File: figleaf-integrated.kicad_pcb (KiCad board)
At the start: 2 copper layers, 145 x 106 mm, 70 parts, among them J1 Conn_01x02_Pin, J2 HRO_TYPE-C-31-M-14, J3 Battery, J9 TC2030_SWD, Q2 2N7002, SW1 PWR, SW2 RST, U1 SRV05-4, U10 MAX17048, U3 BQ24075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

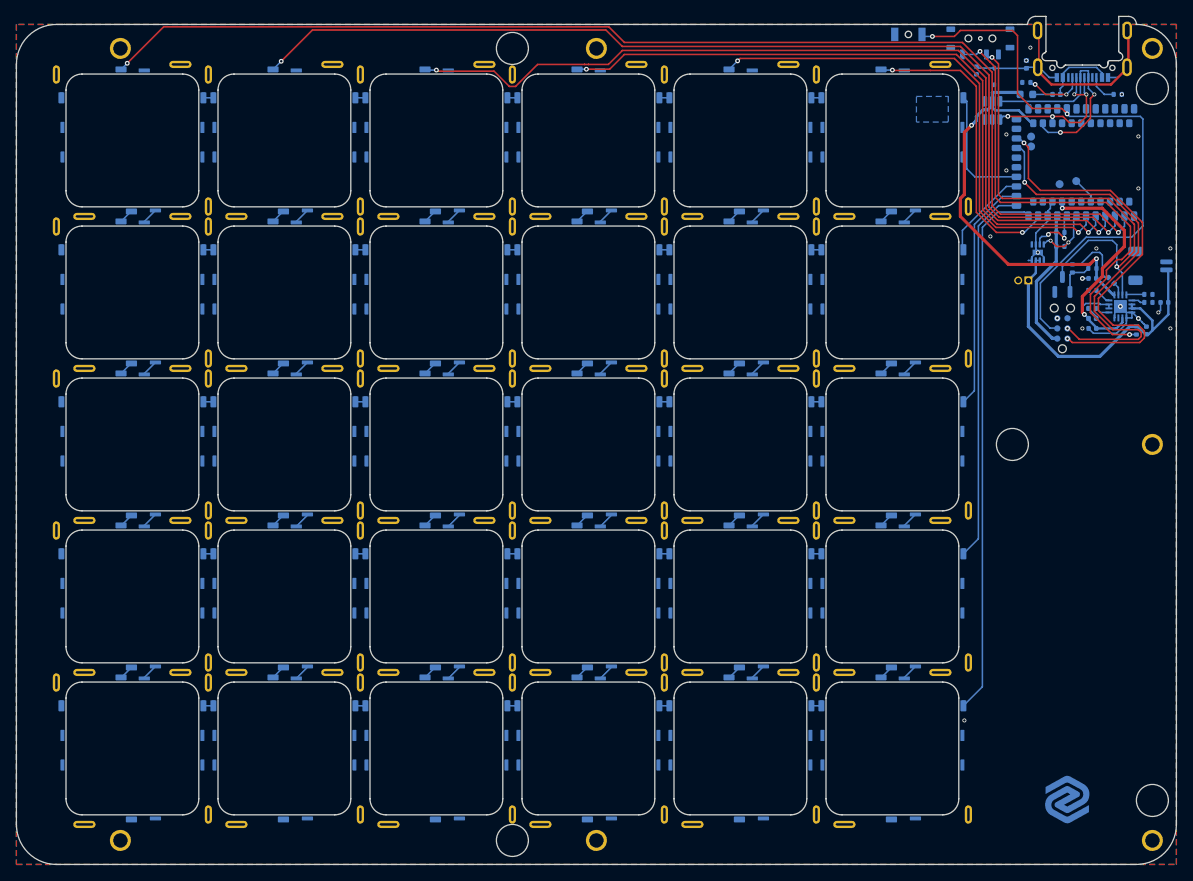
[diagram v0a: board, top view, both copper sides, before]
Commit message: Move LED near antenna
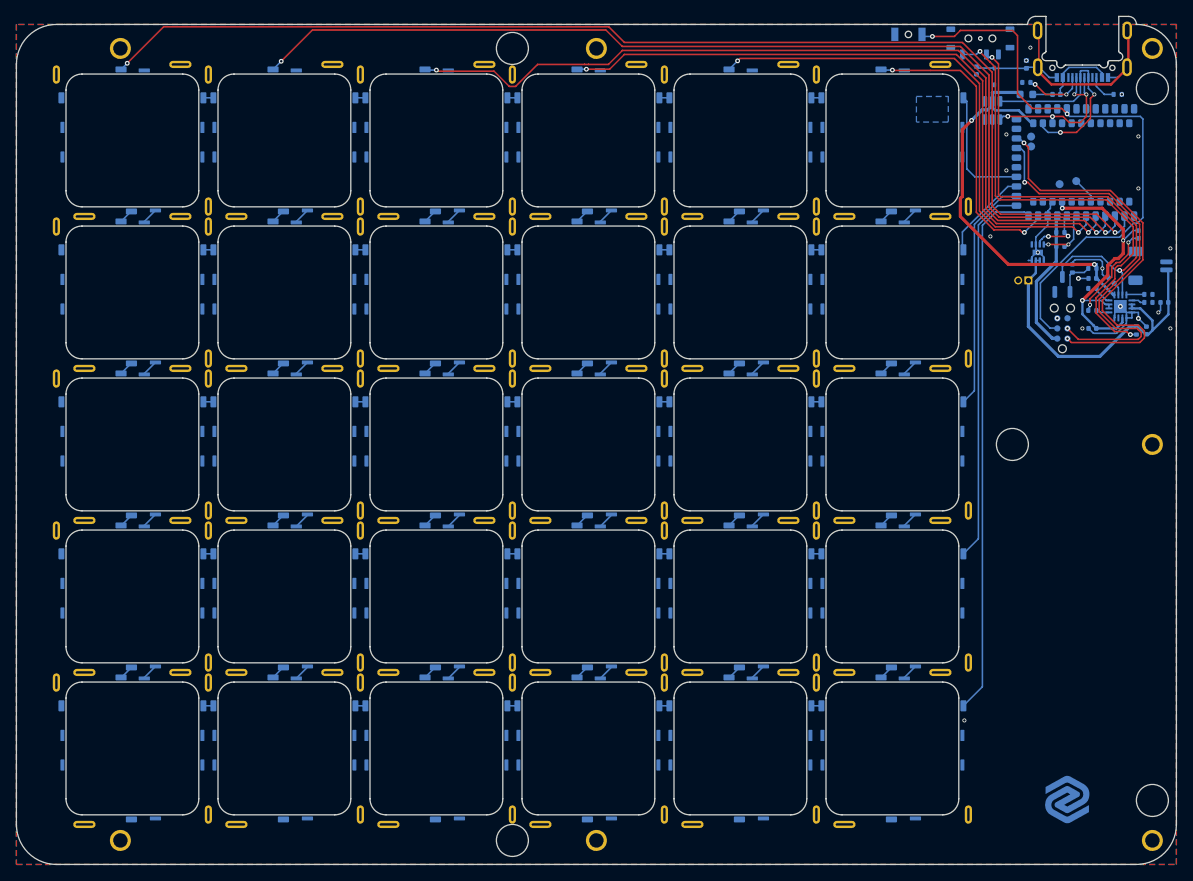
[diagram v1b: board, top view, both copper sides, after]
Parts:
- moved LED2 12.0 mm to (152.7, 38.8), turned to 90 degrees
- moved R10 0.25 mm to (147.0, 48.2)
- moved R12 0.25 mm to (147.0, 45.5)
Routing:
- net Net-(LED2-K): track 1.66 -> 12.0 mm, vias 0 -> 2
- net SYSOFF: track 59.5 -> 56.9 mm
- net +VSW: track 34.1 -> 35.7 mm, vias 2 -> 3
- net +5V: track 53.3 -> 52.3 mm
- net SWDCLK: track 52.1 -> 51.3 mm
- net Net-(SW1-A): track 59.8 -> 59.2 mm
- net RST: track 73.7 -> 73.1 mm
- net SWDIO: track 53.3 -> 52.7 mm
- net SDA: track 8.20 -> 7.65 mm

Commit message: small deets
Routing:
- net RST: track 73.1 -> 72.1 mm

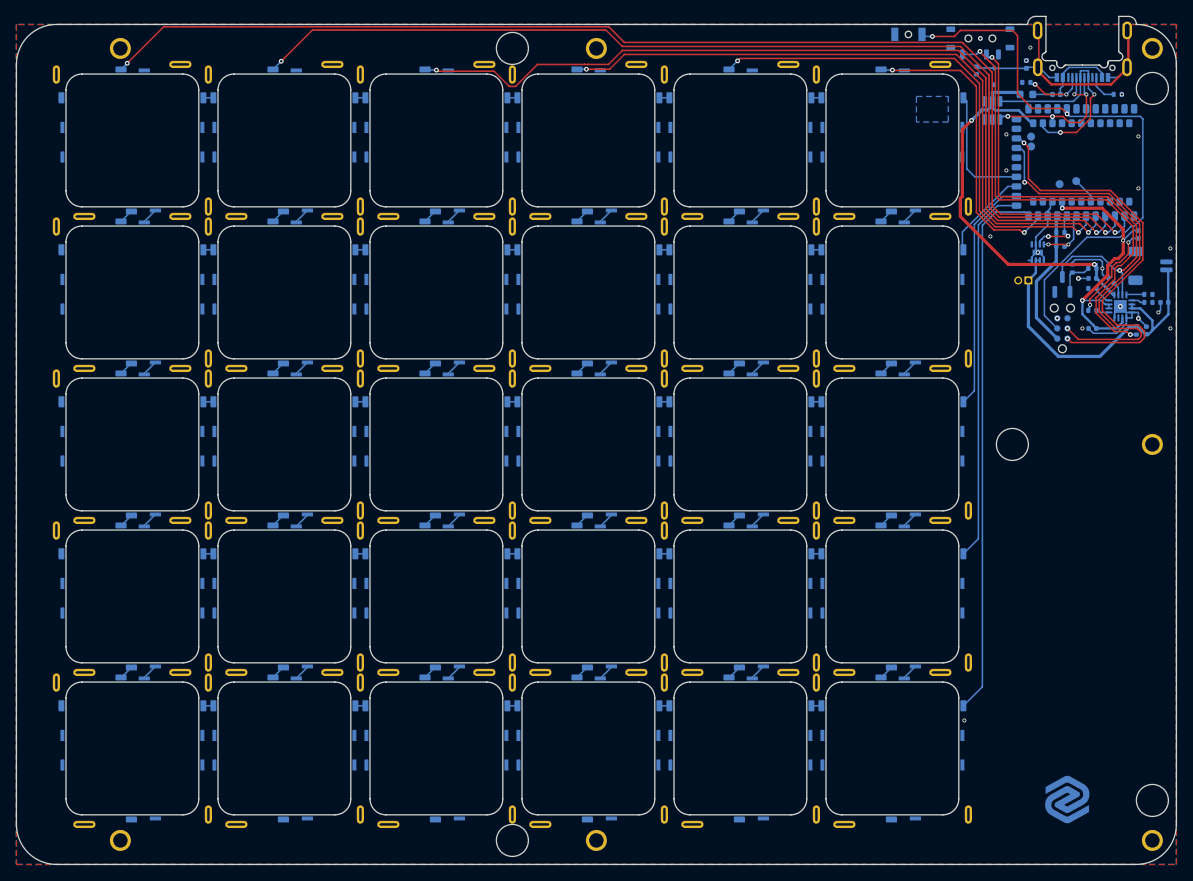
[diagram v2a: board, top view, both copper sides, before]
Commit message: update OKM footprint, larger GND, smaller RADI
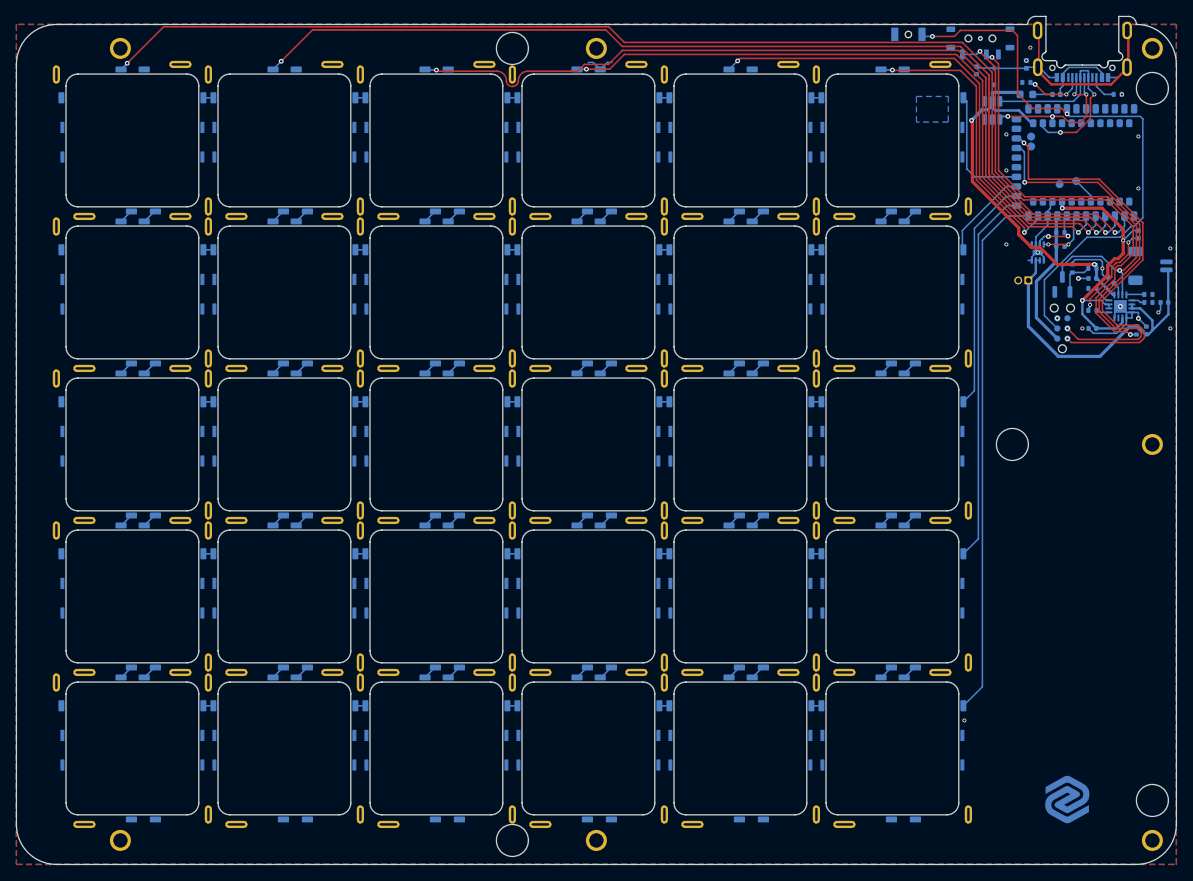
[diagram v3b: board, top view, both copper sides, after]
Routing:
- net +5V: track 52.3 -> 48.2 mm
- net GND_L: track 39.2 -> 42.9 mm
- net col_1: track 129.4 -> 127.0 mm
- net col_0: track 150.0 -> 147.6 mm
- net col_4: track 65.4 -> 63.0 mm
- net col_3: track 85.9 -> 83.5 mm
- net col_5: track 38.3 -> 36.3 mm
- net col_2: track 108.5 -> 106.5 mm
- net Net-(SW1-A): track 59.2 -> 57.4 mm
- net SYSOFF: track 56.9 -> 55.1 mm
- net row_4: track 67.7 -> 66.2 mm
- net row_3: track 47.6 -> 46.9 mm

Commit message: Adding new magnet through holes
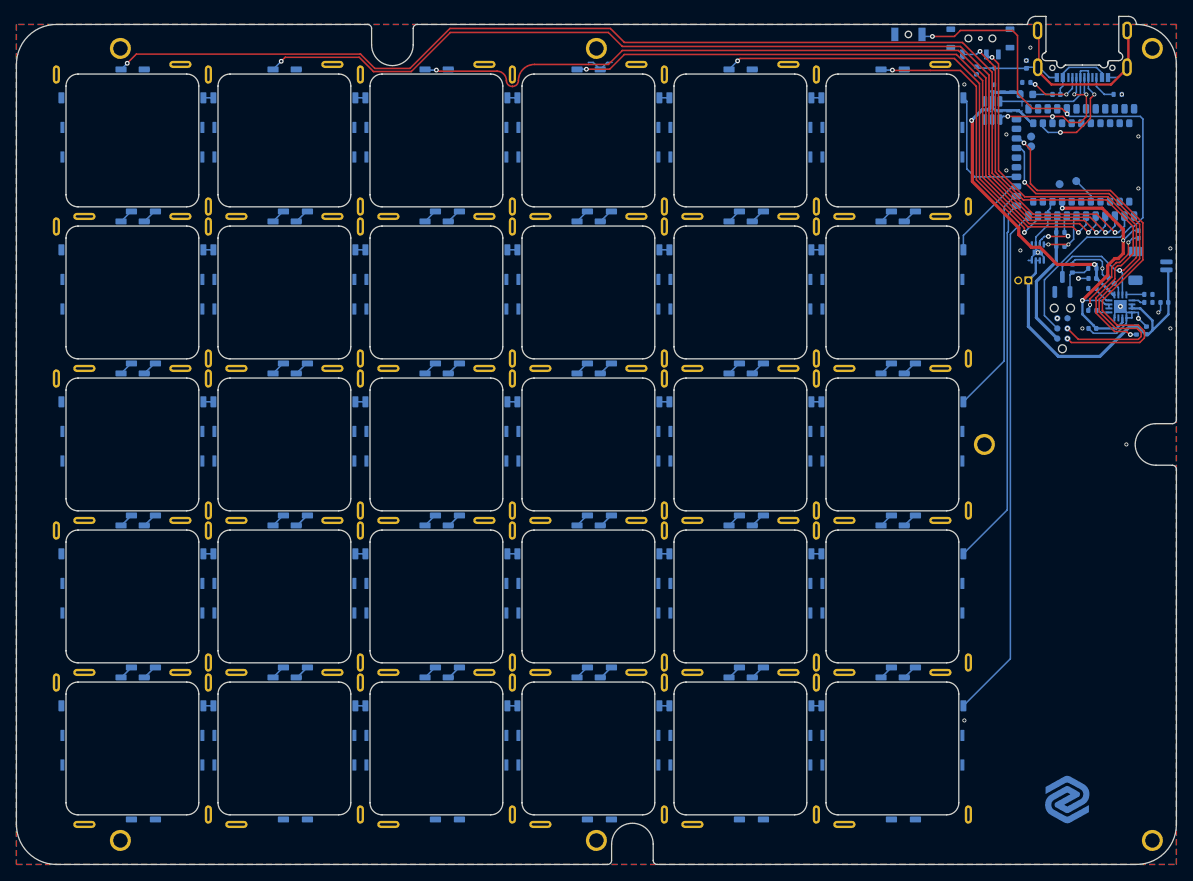
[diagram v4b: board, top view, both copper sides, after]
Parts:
- moved H4 21.0 mm to (133.5, 65.0)
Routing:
- net row_4: track 66.2 -> 64.6 mm
- net col_0: track 147.6 -> 149.0 mm
- net col_1: track 127.0 -> 128.3 mm
- net row_3: track 46.9 -> 46.3 mm
- net row_2: track 29.2 -> 28.6 mm
- net row_1: track 11.5 -> 11.0 mm
- net GND_L: vias 20 -> 22
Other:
- outline, holes or cut-outs redrawn
